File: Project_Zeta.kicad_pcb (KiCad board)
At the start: 2 copper layers, 80 x 80 mm, 26 parts, among them J1 Conn_01x20, J2 Conn_01x20, J3 Screw_Terminal_01x02, J4 Conn_01x08, J5 Conn_01x02, J6 Conn_01x01, J7 Conn_01x01

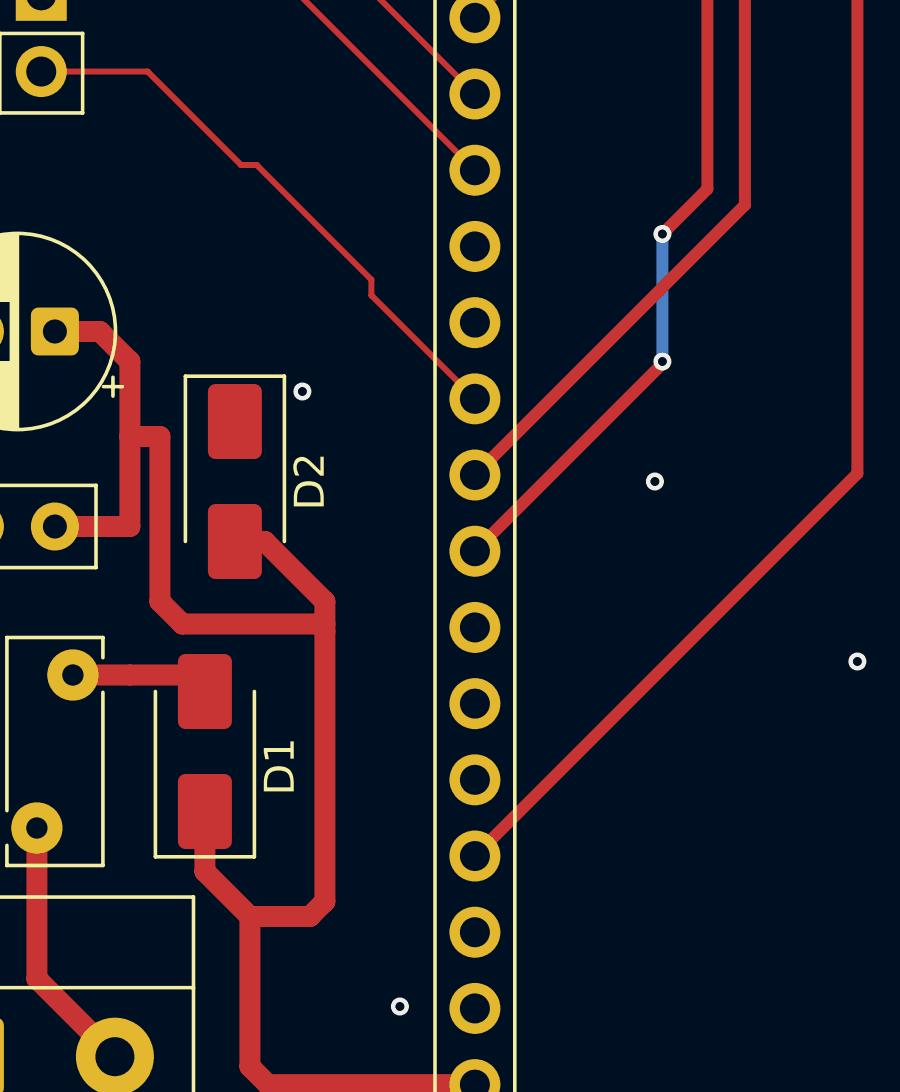
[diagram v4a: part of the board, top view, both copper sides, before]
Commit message: Fix wrong direction Diode
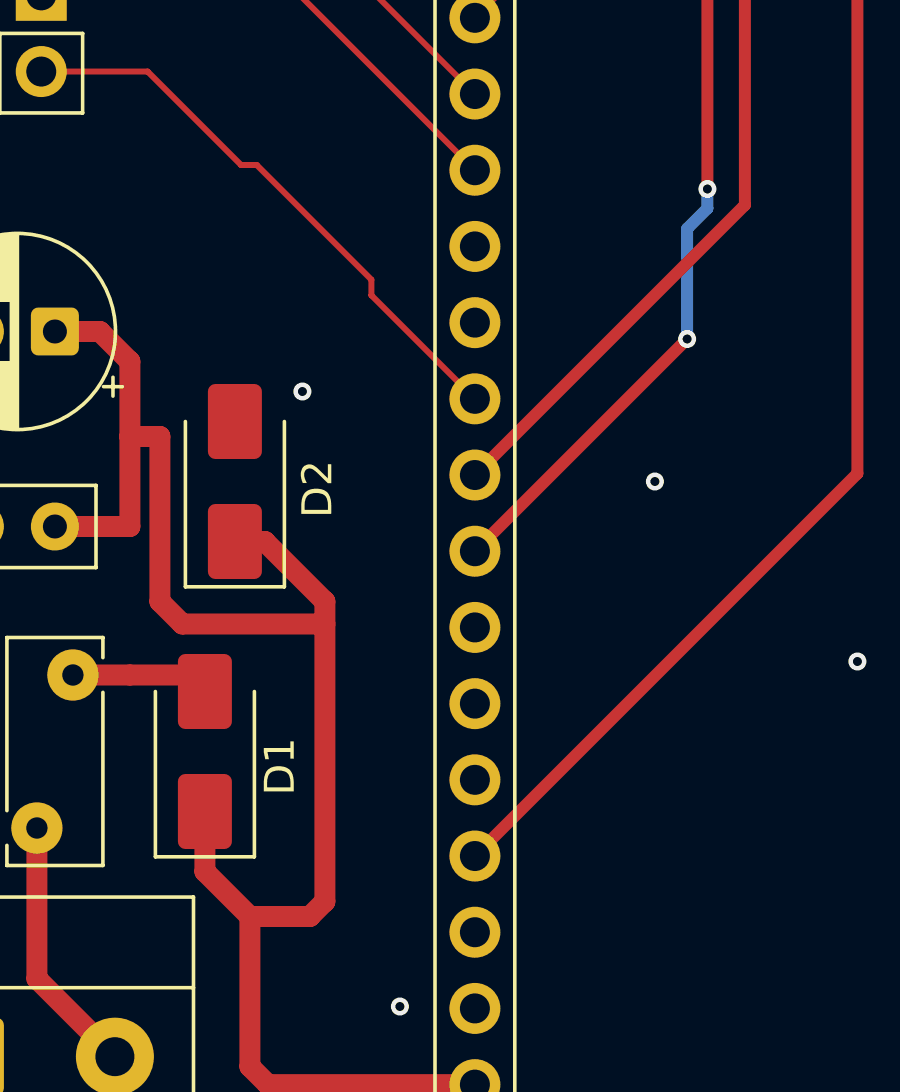
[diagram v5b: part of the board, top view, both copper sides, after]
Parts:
- turned D2 to 90 degrees
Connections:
- D2 pad 1: /VSYS -> GND
- D2 pad 2: GND -> /VSYS
- F1 pad 1: +5V -> unconnected-(F1-Pad1)
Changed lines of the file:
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@@
 			(layers "*.Cu" "*.Mask")
 			(remove_unused_layers no)
-			(net "+5V")
+			(net "unconnected-(F1-Pad1)")
 			(pintype "passive")
 		)
@@
 	(footprint "Diode_SMD:D_SMA"
 		(layer "F.Cu")
-		(at 123.5 103.5 -90)
+		(at 123.5 103.5 90)
 		(descr "Diode SMA (DO-214AC)")
 		(tags "Diode SMA (DO-214AC)")
 		(property "Reference" "D2"
-			(at 0 -2.5 90)
+			(at -0.25 2.75 90)
 			(layer "F.SilkS")
 			(effects
@@
 		)
 		(property "Value" "SMAJ5.0A"
-			(at -5.5 2.5 90)
+			(at 1.75 3.5 90)
 			(layer "F.Fab")
 			(effects
@@
 		)
 		(property "Datasheet" "https://www.littelfuse.com/media?resourcetype=datasheets&itemid=75e32973-b177-4ee3-a0ff-cedaf1abdb93&filename=smaj-datasheet"
-			(at 0 0 270)
+			(at 0 0 90)
 			(unlocked yes)
 			(layer "F.Fab")
@@
 		)
 		(property "Description" "400W unidirectional Transient Voltage Suppressor, 5.0Vr, SMA(DO-214AC)"
-			(at 0 0 270)
+			(at 0 0 90)
 			(unlocked yes)
 			(layer "F.Fab")
@@
 		(duplicate_pad_numbers_are_jumpers no)
 		(fp_line
-			(start -3.51 1.65)
-			(end 2 1.65)
+			(start -3.51 -1.65)
+			(end 2 -1.65)
 			(stroke
 				(width 0.12)
@@
 		)
 		(fp_line
-			(start -3.51 -1.65)
-			(end 2 -1.65)
+			(start -3.51 1.65)
+			(end 2 1.65)
 			(stroke
 				(width 0.12)
@@
 		)
 		(fp_line
-			(start -3.5 1.75)
-			(end -3.5 -1.75)
+			(start 3.5 -1.75)
+			(end 3.5 1.75)
 			(stroke
 				(width 0.05)
@@
 		)
 		(fp_line
-			(start 3.5 1.75)
-			(end -3.5 1.75)
+			(start -3.5 -1.75)
+			(end 3.5 -1.75)
 			(stroke
 				(width 0.05)
@@
 		)
 		(fp_line
-			(start -3.5 -1.75)
-			(end 3.5 -1.75)
+			(start 3.5 1.75)
+			(end -3.5 1.75)
 			(stroke
 				(width 0.05)
@@
 		)
 		(fp_line
-			(start 3.5 -1.75)
-			(end 3.5 1.75)
+			(start -3.5 1.75)
+			(end -3.5 -1.75)
 			(stroke
 				(width 0.05)
@@
 		)
 		(fp_line
-			(start -2.3 1.5)
+			(start 2.3 -1.5)
 			(end -2.3 -1.5)
 			(stroke
@@
 		)
 		(fp_line
-			(start 2.3 1.5)
-			(end -2.3 1.5)
+			(start 2.3 -1.5)
+			(end 2.3 1.5)
 			(stroke
 				(width 0.1)
@@
 		)
 		(fp_line
-			(start 0.50118 0.75032)
-			(end 0.50118 -0.79908)
+			(start -0.64944 -0.79908)
+			(end -0.64944 0.80112)
 			(stroke
 				(width 0.1)
@@
 		)
 		(fp_line
-			(start -0.64944 0.00102)
-			(end 0.50118 0.75032)
+			(start 0.50118 0.00102)
+			(end 1.4994 0.00102)
 			(stroke
 				(width 0.1)
@@
 		(fp_line
 			(start -0.64944 0.00102)
-			(end -1.55114 0.00102)
+			(end 0.50118 -0.79908)
 			(stroke
 				(width 0.1)
@@
 		(fp_line
 			(start -0.64944 0.00102)
-			(end 0.50118 -0.79908)
+			(end -1.55114 0.00102)
 			(stroke
 				(width 0.1)
@@
 		)
 		(fp_line
-			(start 0.50118 0.00102)
-			(end 1.4994 0.00102)
+			(start -0.64944 0.00102)
+			(end 0.50118 0.75032)
 			(stroke
 				(width 0.1)
@@
 		)
 		(fp_line
-			(start -0.64944 -0.79908)
-			(end -0.64944 0.80112)
+			(start 0.50118 0.75032)
+			(end 0.50118 -0.79908)
 			(stroke
 				(width 0.1)
@@
 		)
 		(fp_line
-			(start 2.3 -1.5)
-			(end 2.3 1.5)
+			(start 2.3 1.5)
+			(end -2.3 1.5)
 			(stroke
 				(width 0.1)
@@
 		)
 		(fp_line
-			(start 2.3 -1.5)
+			(start -2.3 1.5)
 			(end -2.3 -1.5)
 			(stroke
@@
 		)
 		(pad "1" smd roundrect
-			(at 2 0 270)
+			(at 2 0 90)
 			(size 2.5 1.8)
 			(layers "F.Cu" "F.Mask" "F.Paste")
 			(roundrect_rratio 0.1388888889)
-			(net "/VSYS")
+			(net "GND")
 			(pinfunction "A1_1")
 			(pintype "passive")
 		)
 		(pad "2" smd roundrect
-			(at -2 0 270)
+			(at -2 0 90)
 			(size 2.5 1.8)
 			(layers "F.Cu" "F.Mask" "F.Paste")
 			(roundrect_rratio 0.1388888889)
-			(net "GND")
+			(net "/VSYS")
 			(pinfunction "A2_2")
 			(pintype "passive")
@@
 	)
 	(segment
+		(start 159.6 115.6)
+		(end 159 115)
+		(width 0.7)
+		(layer "F.Cu")
+		(net "Net-(D3-A)")
+	)
+	(segment
+		(start 159.6 117.95)
+		(end 159.6 115.6)
+		(width 0.7)
+		(layer "F.Cu")
+		(net "Net-(D3-A)")
+	)
+	(segment
 		(start 158.5 127.5)
 		(end 158.5 123.15)
@@
 	)
 	(segment
-		(start 159.6 115.6)
-		(end 159 115)
+		(start 121.75 108.25)
+		(end 121 107.5)
 		(width 0.7)
 		(layer "F.Cu")
-		(net "Net-(D3-A)")
+		(net "/VSYS")
 	)
 	(segment
-		(start 159.6 117.95)
-		(end 159.6 115.6)
+		(start 126.5 117.5)
+		(end 126.5 107.5)
 		(width 0.7)
 		(layer "F.Cu")
-		(net "Net-(D3-A)")
+		(net "/VSYS")
 	)
 	(segment
-		(start 121.75 108.25)
-		(end 121 107.5)
+		(start 124.5 105.5)
+		(end 123.5 105.5)
 		(width 0.7)
 		(layer "F.Cu")
@@
 	)
 	(segment
-		(start 121 107.5)
-		(end 121 102)
+		(start 126 118)
+		(end 126.5 117.5)
 		(width 0.7)
 		(layer "F.Cu")
@@
 	)
 	(segment
-		(start 120 105)
-		(end 117.5 105)
+		(start 126.5 107.5)
+		(end 124.5 105.5)
 		(width 0.7)
 		(layer "F.Cu")
@@
 	)
 	(segment
-		(start 124 118)
-		(end 126 118)
+		(start 121 107.5)
+		(end 121 102)
 		(width 0.7)
 		(layer "F.Cu")
@@
 	)
 	(segment
-		(start 126.5 107.5)
-		(end 124.5 105.5)
+		(start 120 105)
+		(end 117.5 105)
 		(width 0.7)
 		(layer "F.Cu")
@@
 	)
 	(segment
-		(start 126.5 117.5)
-		(end 126.5 108.5)
-		(width 0.7)
-		(layer "F.Cu")
-		(net "/VSYS")
-	)
-	(segment
 		(start 120 99.5)
 		(end 120 102)
@@
 	)
 	(segment
+		(start 124 118)
+		(end 126 118)
+		(width 0.7)
+		(layer "F.Cu")
+		(net "/VSYS")
+	)
+	(segment
 		(start 119 98.5)
 		(end 120 99.5)
@@
 	)
 	(segment
-		(start 126.5 108.5)
-		(end 126.5 107.5)
-		(width 0.7)
-		(layer "F.Cu")
-		(net "/VSYS")
-	)
-	(segment
 		(start 120 102)
 		(end 120 105)
@@
 	)
 	(segment
-		(start 124.5 105.5)
-		(end 123.5 105.5)
-		(width 0.7)
-		(layer "F.Cu")
-		(net "/VSYS")
-	)
-	(segment
-		(start 126 118)
-		(end 126.5 117.5)
-		(width 0.7)
-		(layer "F.Cu")
-		(net "/VSYS")
-	)
-	(segment
 		(start 169.75 71.75)
 		(end 171.5 70)
@@
 	)
 	(segment
-		(start 148.5 70.75)
-		(end 149.5 70.75)
-		(width 0.4)
-		(layer "F.Cu")
-		(net "/GP27")
-	)
-	(segment
-		(start 131.5 105.824282)
-		(end 137.75 99.574282)
+		(start 139.25 93.75)
+		(end 139.25 75)
 		(width 0.4)
 		(layer "F.Cu")
@@
 	)
 	(segment
-		(start 166.25 70.25)
-		(end 171.5 65)
+		(start 148.5 70.75)
+		(end 149.5 70.75)
 		(width 0.4)
 		(layer "F.Cu")
@@
 	)
 	(segment
-		(start 137.75 95.25)
-		(end 139.25 93.75)
+		(start 166.25 70.25)
+		(end 171.5 65)
 		(width 0.4)
 		(layer "F.Cu")
@@
 	)
 	(segment
-		(start 137.75 99.574282)
-		(end 137.75 99.5)
-		(width 0.2)
+		(start 138.574282 98.75)
+		(end 131.5 105.824282)
+		(width 0.4)
 		(layer "F.Cu")
 		(net "/GP27")
@@
 		(net "/GP27")
 	)
-	(segment
-		(start 139.25 93.75)
-		(end 139.25 75)
-		(width 0.4)
-		(layer "F.Cu")
-		(net "/GP27")
-	)
 	(via
-		(at 137.75 99.5)
+		(at 138.574282 98.75)
 		(size 0.6)
 		(drill 0.3)
@@
 	)
 	(via
-		(at 137.75 95.25)
+		(at 139.25 93.75)
 		(size 0.6)
 		(drill 0.3)
@@
 	)
 	(segment
+		(start 138.574282 95.074282)
+		(end 138.574282 98.75)
+		(width 0.4)
+		(layer "B.Cu")
+		(net "/GP27")
+	)
+	(segment
 		(start 144.75 74.5)
 		(end 145.5 73.75)
@@
 	)
 	(segment
+		(start 139.25 93.75)
+		(end 139.25 94.398564)
+		(width 0.4)
+		(layer "B.Cu")
+		(net "/GP27")
+	)
+	(segment
 		(start 139.75 74.5)
 		(end 144.75 74.5)
@@
 	)
 	(segment
-		(start 137.75 99.5)
-		(end 137.75 95.25)
+		(start 139.25 94.398564)
+		(end 138.574282 95.074282)
 		(width 0.4)
 		(layer "B.Cu")
@@
 	)
 	(segment
+		(start 116.9 120.0725)
+		(end 116.9 115.05)
+		(width 0.7)
+		(layer "F.Cu")
+		(net "+5V")
+	)
+	(segment
+		(start 119.5 122.6725)
+		(end 116.9 120.0725)
+		(width 0.7)
+		(layer "F.Cu")
+		(net "+5V")
+	)
+	(segment
 		(start 149.282934 85.51675)
 		(end 151.376184 87.61)
@@
 		(net "/GP8")
 	)
-	(segment
-		(start 116.9 120.0725)
-		(end 116.9 115.05)
-		(width 0.7)
-		(layer "F.Cu")
-		(net "+5V")
-	)
-	(segment
-		(start 119.5 122.6725)
-		(end 116.9 120.0725)
-		(width 0.7)
-		(layer "F.Cu")
-		(net "+5V")
-	)
 	(zone

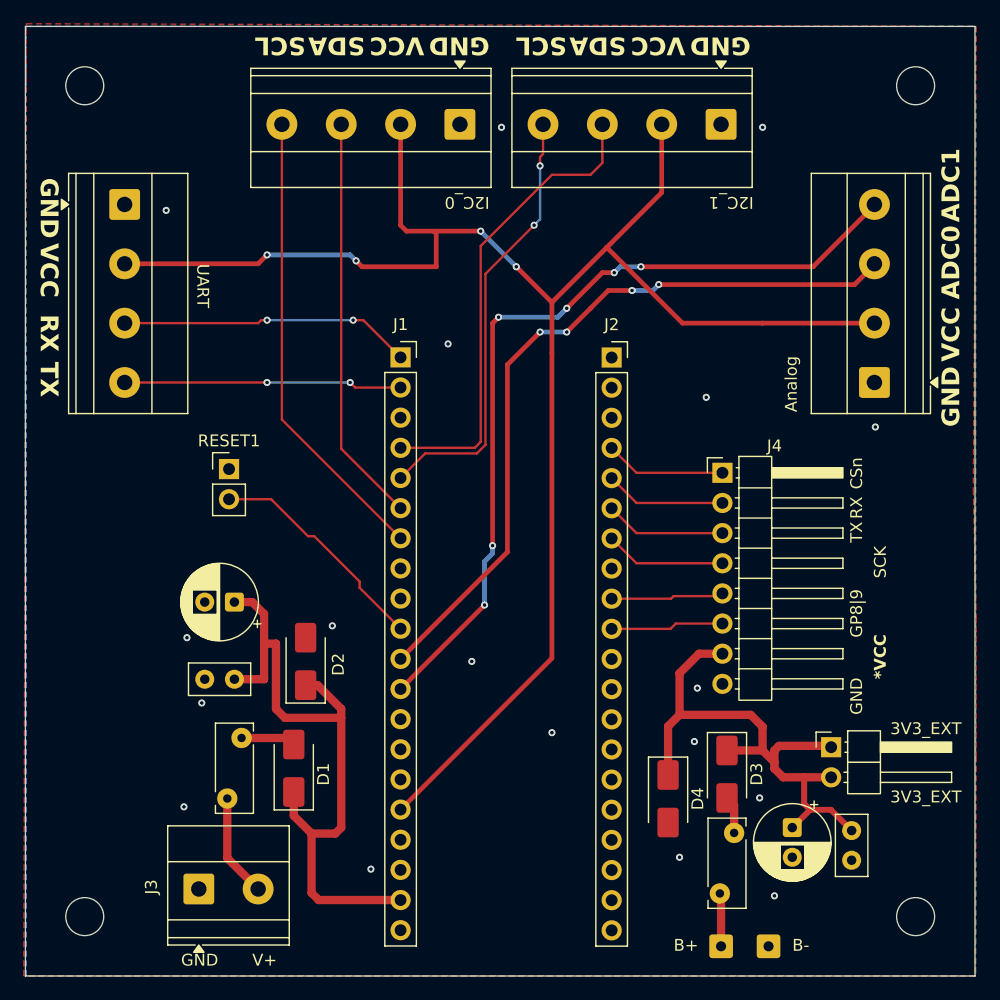
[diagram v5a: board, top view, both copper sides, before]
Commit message: Fix some schematic and add Gas Discharge Tube from GND to Earth
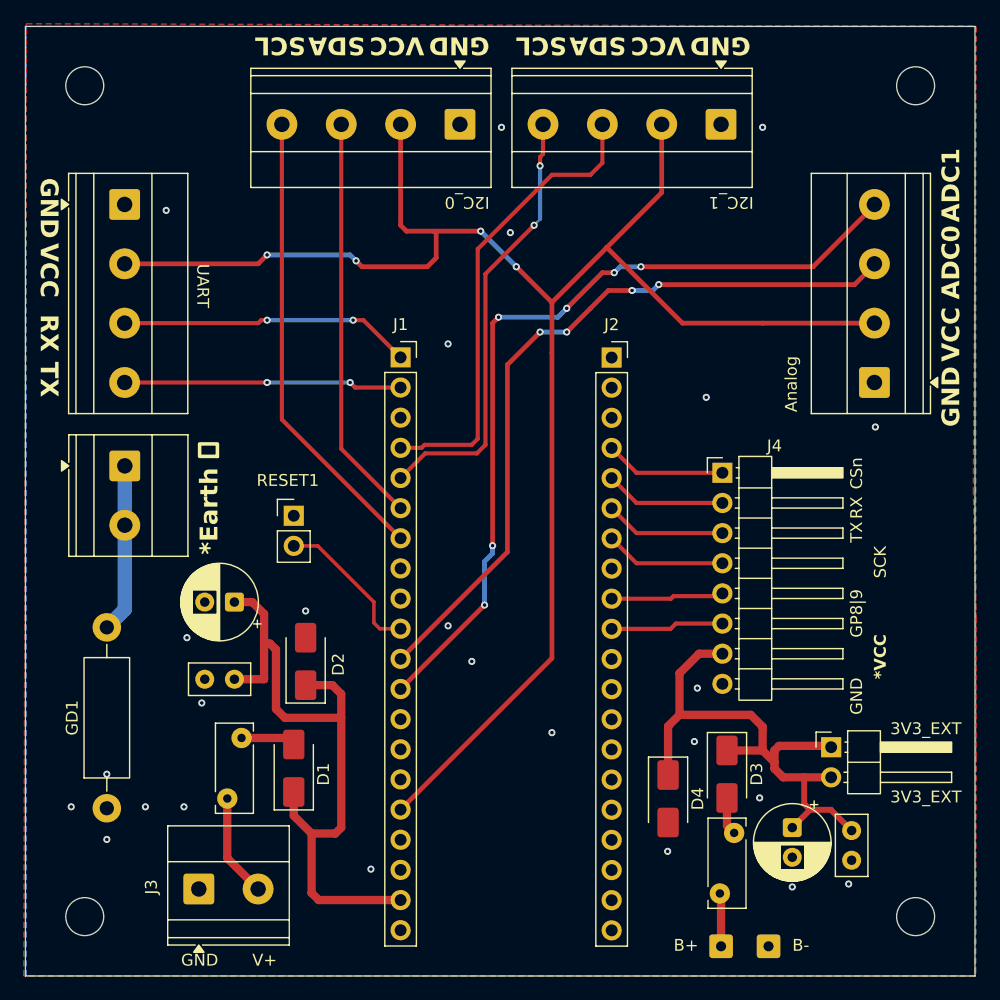
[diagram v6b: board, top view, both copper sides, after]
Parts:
- added GD1: GDT_2Pin, Resistor_THT:R_Axial_DIN0411_L9.9mm_D3.6mm_P15.24mm_Horizontal, F.Cu at (106.8, 115.9)
- added J8: Screw_Terminal_01x02, TerminalBlock_Phoenix:TerminalBlock_Phoenix_MKDS-1,5-2_1x02_P5.00mm_Horizontal, F.Cu at (108.3, 87.0)
- moved RESET1 6.72 mm to (122.5, 91.2)
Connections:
- D2 pad 1: GND -> /VSYS
- D2 pad 2: /VSYS -> GND
- F1 pad 1: unconnected-(F1-Pad1) -> +5V
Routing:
- net Earth_Clean: track 0.00 -> 14.2 mm
- net /RUN: track 19.3 -> 12.9 mm
- net GND: vias 18 -> 25
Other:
- board text added: "*Earth ⏚"

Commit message: Fix some point
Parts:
- moved D1 0.50 mm to (122.5, 113.0)
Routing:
- net /3V3_EXT: track 48.0 -> 61.1 mm
- net /VSYS: track 57.1 -> 45.0 mm
- net GND: vias 25 -> 26
